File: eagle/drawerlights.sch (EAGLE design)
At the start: 12 parts

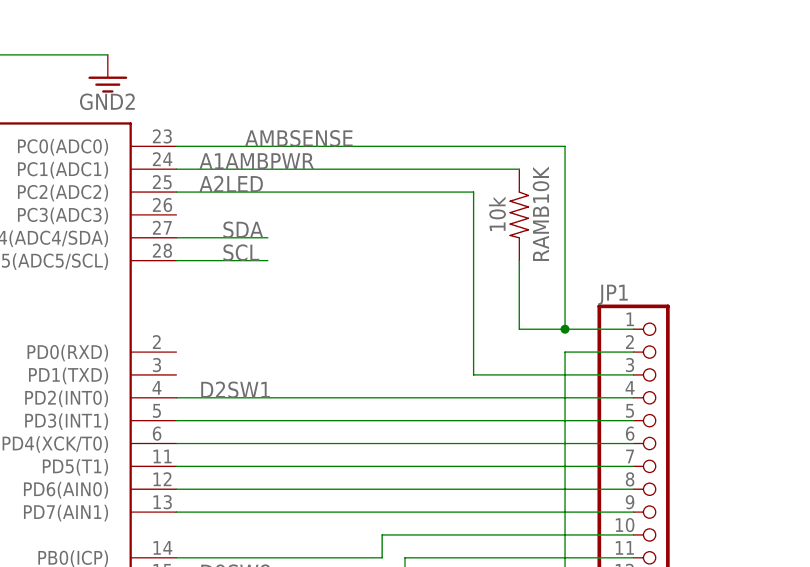
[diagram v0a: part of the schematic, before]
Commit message: add missing resistor for LED control
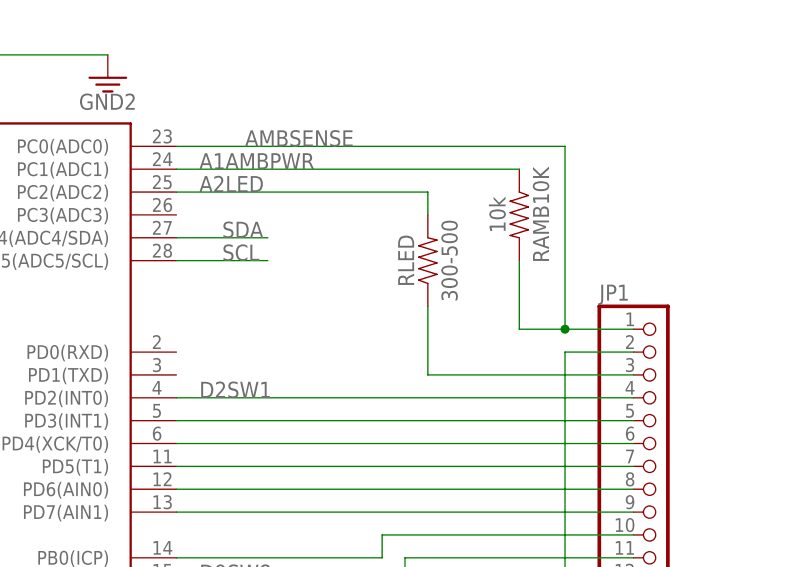
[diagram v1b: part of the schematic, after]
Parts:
- added RLED: 300-500, SparkFun-Resistors:330OHM-HORIZ-1/10W-5%
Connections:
- new net N$1: JP1.3, RLED.1
- net A2LED: now also RLED.2; no longer JP1.3
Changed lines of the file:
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@@
 <part name="LEDPWR" library="SparkFun-Connectors" deviceset="CONN_02" device=""/>
 <part name="C1" library="SparkFun-Capacitors" deviceset="100UF-POLAR" device="-RADIAL-2.5MM-25V-20%" value="100uF"/>
+<part name="RLED" library="SparkFun-Resistors" deviceset="330OHM" device="-HORIZ-1/10W-5%" value="300-500"/>
 </parts>
 <sheets>
@@
 <instance part="LEDPWR" gate="G$1" x="71.12" y="109.22"/>
 <instance part="C1" gate="G$1" x="83.82" y="119.38" rot="R90"/>
+<instance part="RLED" gate="G$1" x="99.06" y="71.12" rot="R90"/>
 </instances>
 <busses>
@@
 <segment>
 <pinref part="ATMEGA328" gate="G$1" pin="PC2(ADC2)"/>
-<wire x1="71.12" y1="78.74" x2="104.14" y2="78.74" width="0.1524" layer="91"/>
+<wire x1="71.12" y1="78.74" x2="99.06" y2="78.74" width="0.1524" layer="91"/>
 <label x="73.66" y="78.74" size="1.778" layer="95"/>
-<wire x1="104.14" y1="78.74" x2="104.14" y2="58.42" width="0.1524" layer="91"/>
-<pinref part="JP1" gate="G$1" pin="3"/>
-<wire x1="104.14" y1="58.42" x2="121.92" y2="58.42" width="0.1524" layer="91"/>
+<pinref part="RLED" gate="G$1" pin="2"/>
+<wire x1="99.06" y1="76.2" x2="99.06" y2="78.74" width="0.1524" layer="91"/>
 </segment>
 </net>
@@
 </segment>
 </net>
+<net name="N$1" class="0">
+<segment>
+<pinref part="JP1" gate="G$1" pin="3"/>
+<wire x1="99.06" y1="58.42" x2="121.92" y2="58.42" width="0.1524" layer="91"/>
+<pinref part="RLED" gate="G$1" pin="1"/>
+<wire x1="99.06" y1="66.04" x2="99.06" y2="58.42" width="0.1524" layer="91"/>
+</segment>
+</net>

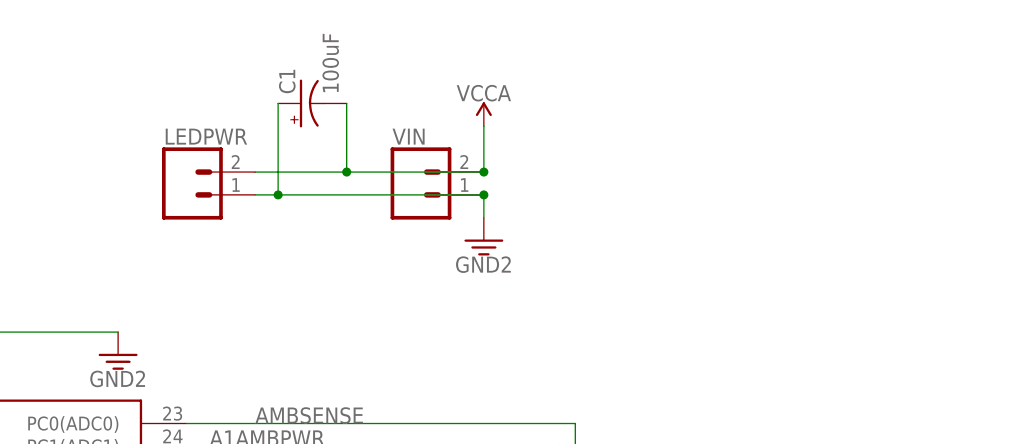
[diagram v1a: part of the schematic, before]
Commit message: fix vcc and LED power and filter cap polarity
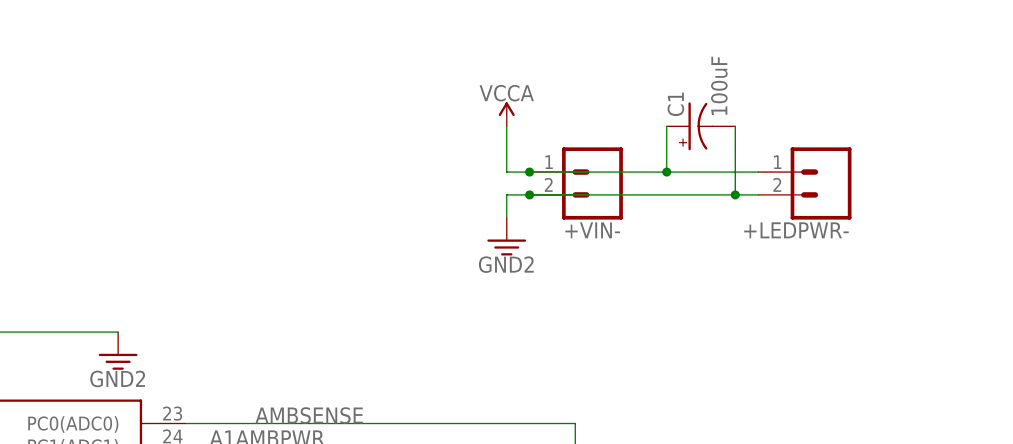
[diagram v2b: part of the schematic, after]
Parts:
- removed LEDPWR, VIN: (no value), SparkFun-Connectors:CONN_02
- added +LEDPWR-, +VIN-: (no value), SparkFun-Connectors:CONN_02
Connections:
- net GND: now also +LEDPWR-.2, +VIN-.2, C1.-; no longer C1.+, LEDPWR.1, VIN.1
- net VCCA: now also +LEDPWR-.1, +VIN-.1, C1.+; no longer C1.-, LEDPWR.2, VIN.2
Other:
- moved on the sheet: C1
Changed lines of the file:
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@@
 <part name="U$2" library="SparkFun-PowerSymbols" deviceset="VCCA" device=""/>
 <part name="SUPPLY4" library="SparkFun-PowerSymbols" deviceset="GND2" device=""/>
-<part name="VIN" library="SparkFun-Connectors" deviceset="CONN_02" device=""/>
+<part name="+VIN-" library="SparkFun-Connectors" deviceset="CONN_02" device=""/>
 <part name="SUPPLY6" library="SparkFun-PowerSymbols" deviceset="GND2" device=""/>
 <part name="RAMB10K" library="SparkFun-Resistors" deviceset="10KOHM" device="-HORIZ-1/4W-1%" value="10k"/>
@@
 <part name="JP1" library="adafruit" deviceset="PINHD-1X12" device="-CB"/>
 <part name="SUPPLY3" library="SparkFun-PowerSymbols" deviceset="GND2" device=""/>
-<part name="LEDPWR" library="SparkFun-Connectors" deviceset="CONN_02" device=""/>
+<part name="+LEDPWR-" library="SparkFun-Connectors" deviceset="CONN_02" device=""/>
 <part name="C1" library="SparkFun-Capacitors" deviceset="100UF-POLAR" device="-RADIAL-2.5MM-25V-20%" value="100uF"/>
 <part name="RLED" library="SparkFun-Resistors" deviceset="330OHM" device="-HORIZ-1/10W-5%" value="300-500"/>
@@
 <instance part="VCC" gate="G$1" x="5.08" y="83.82"/>
 <instance part="U$2" gate="G$1" x="12.7" y="96.52"/>
-<instance part="SUPPLY4" gate="GND" x="104.14" y="104.14"/>
-<instance part="VIN" gate="G$1" x="96.52" y="109.22"/>
+<instance part="SUPPLY4" gate="GND" x="106.68" y="104.14"/>
+<instance part="+VIN-" gate="G$1" x="116.84" y="111.76" rot="R180"/>
 <instance part="SUPPLY6" gate="GND" x="63.5" y="91.44"/>
 <instance part="RAMB10K" gate="G$1" x="109.22" y="76.2" rot="R270"/>
@@
 <instance part="TPDIV" gate="G$1" x="160.02" y="38.1"/>
 <instance part="TPVREG" gate="G$1" x="160.02" y="60.96"/>
-<instance part="U$1" gate="G$1" x="104.14" y="116.84"/>
+<instance part="U$1" gate="G$1" x="106.68" y="116.84"/>
 <instance part="JP1" gate="G$1" x="124.46" y="50.8"/>
 <instance part="SUPPLY3" gate="GND" x="114.3" y="33.02"/>
-<instance part="LEDPWR" gate="G$1" x="71.12" y="109.22"/>
-<instance part="C1" gate="G$1" x="83.82" y="119.38" rot="R90"/>
+<instance part="+LEDPWR-" gate="G$1" x="142.24" y="111.76" rot="R180"/>
+<instance part="C1" gate="G$1" x="127" y="116.84" rot="R90"/>
 <instance part="RLED" gate="G$1" x="99.06" y="71.12" rot="R90"/>
 </instances>
@@
 </segment>
 <segment>
-<pinref part="VIN" gate="G$1" pin="2"/>
+<pinref part="+VIN-" gate="G$1" pin="1"/>
+<wire x1="109.22" y1="111.76" x2="106.68" y2="111.76" width="0.1524" layer="91"/>
 <pinref part="U$1" gate="G$1" pin="VCCA"/>
-<wire x1="104.14" y1="111.76" x2="104.14" y2="116.84" width="0.1524" layer="91"/>
-<pinref part="LEDPWR" gate="G$1" pin="2"/>
-<wire x1="104.14" y1="111.76" x2="88.9" y2="111.76" width="0.1524" layer="91"/>
-<junction x="104.14" y="111.76"/>
-<pinref part="C1" gate="G$1" pin="-"/>
-<wire x1="88.9" y1="111.76" x2="78.74" y2="111.76" width="0.1524" layer="91"/>
-<wire x1="88.9" y1="119.38" x2="88.9" y2="111.76" width="0.1524" layer="91"/>
-<junction x="88.9" y="111.76"/>
+<wire x1="106.68" y1="111.76" x2="106.68" y2="116.84" width="0.1524" layer="91"/>
+<pinref part="+LEDPWR-" gate="G$1" pin="1"/>
+<wire x1="109.22" y1="111.76" x2="124.46" y2="111.76" width="0.1524" layer="91"/>
+<junction x="109.22" y="111.76"/>
+<pinref part="C1" gate="G$1" pin="+"/>
+<wire x1="124.46" y1="111.76" x2="134.62" y2="111.76" width="0.1524" layer="91"/>
+<wire x1="124.46" y1="116.84" x2="124.46" y2="111.76" width="0.1524" layer="91"/>
+<junction x="124.46" y="111.76"/>
 </segment>
 </net>
@@
 </segment>
 <segment>
-<pinref part="VIN" gate="G$1" pin="1"/>
-<pinref part="SUPPLY4" gate="GND" pin="3.3V"/>
-<wire x1="104.14" y1="109.22" x2="104.14" y2="106.68" width="0.1524" layer="91"/>
-<pinref part="LEDPWR" gate="G$1" pin="1"/>
-<wire x1="104.14" y1="109.22" x2="81.28" y2="109.22" width="0.1524" layer="91"/>
-<junction x="104.14" y="109.22"/>
-<pinref part="C1" gate="G$1" pin="+"/>
-<wire x1="81.28" y1="109.22" x2="78.74" y2="109.22" width="0.1524" layer="91"/>
-<wire x1="81.28" y1="119.38" x2="81.28" y2="109.22" width="0.1524" layer="91"/>
-<junction x="81.28" y="109.22"/>
-</segment>
-<segment>
 <pinref part="JP1" gate="G$1" pin="12"/>
 <pinref part="SUPPLY3" gate="GND" pin="3.3V"/>
@@
 <junction x="114.3" y="35.56"/>
 </segment>
+<segment>
+<pinref part="SUPPLY4" gate="GND" pin="3.3V"/>
+<wire x1="106.68" y1="106.68" x2="106.68" y2="109.22" width="0.1524" layer="91"/>
+<pinref part="+VIN-" gate="G$1" pin="2"/>
+<wire x1="109.22" y1="109.22" x2="106.68" y2="109.22" width="0.1524" layer="91"/>
+<pinref part="+LEDPWR-" gate="G$1" pin="2"/>
+<wire x1="134.62" y1="109.22" x2="132.08" y2="109.22" width="0.1524" layer="91"/>
+<junction x="109.22" y="109.22"/>
+<pinref part="C1" gate="G$1" pin="-"/>
+<wire x1="132.08" y1="109.22" x2="109.22" y2="109.22" width="0.1524" layer="91"/>
+<wire x1="132.08" y1="116.84" x2="132.08" y2="109.22" width="0.1524" layer="91"/>
+<junction x="132.08" y="109.22"/>
+</segment>
 </net>

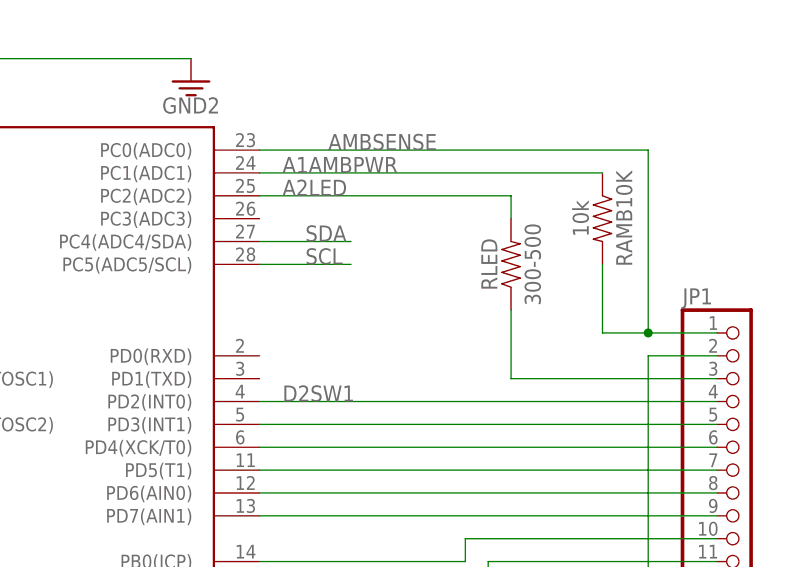
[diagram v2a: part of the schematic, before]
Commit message: move LED control to D0, fix # LEDs per drawer 4 => 8
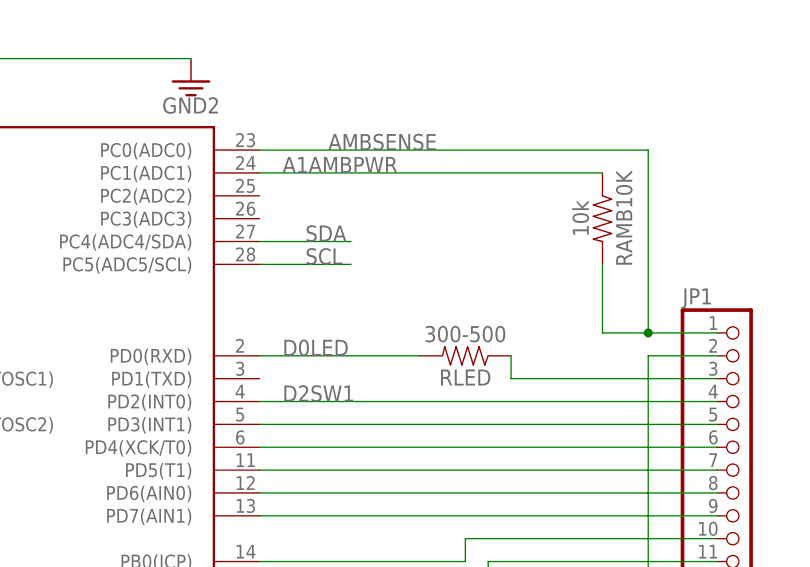
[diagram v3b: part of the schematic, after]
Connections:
- removed net A2LED: ATMEGA328.PC2(ADC2), RLED.2
- new net D0LED: ATMEGA328.PD0(RXD), RLED.2
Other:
- moved on the sheet: RLED
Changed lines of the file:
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@@
 <instance part="+LEDPWR-" gate="G$1" x="142.24" y="111.76" rot="R180"/>
 <instance part="C1" gate="G$1" x="127" y="116.84" rot="R90"/>
-<instance part="RLED" gate="G$1" x="99.06" y="71.12" rot="R90"/>
+<instance part="RLED" gate="G$1" x="93.98" y="60.96" rot="R180"/>
 </instances>
 <busses>
@@
 </segment>
 </net>
-<net name="A2LED" class="0">
-<segment>
-<pinref part="ATMEGA328" gate="G$1" pin="PC2(ADC2)"/>
-<wire x1="71.12" y1="78.74" x2="99.06" y2="78.74" width="0.1524" layer="91"/>
-<label x="73.66" y="78.74" size="1.778" layer="95"/>
-<pinref part="RLED" gate="G$1" pin="2"/>
-<wire x1="99.06" y1="76.2" x2="99.06" y2="78.74" width="0.1524" layer="91"/>
-</segment>
-</net>
 <net name="D2SW1" class="0">
 <segment>
@@
 <wire x1="99.06" y1="58.42" x2="121.92" y2="58.42" width="0.1524" layer="91"/>
 <pinref part="RLED" gate="G$1" pin="1"/>
-<wire x1="99.06" y1="66.04" x2="99.06" y2="58.42" width="0.1524" layer="91"/>
-</segment>
-</net>
+<wire x1="99.06" y1="60.96" x2="99.06" y2="58.42" width="0.1524" layer="91"/>
+</segment>
+</net>
+<net name="D0LED" class="0">
+<segment>
+<pinref part="RLED" gate="G$1" pin="2"/>
+<pinref part="ATMEGA328" gate="G$1" pin="PD0(RXD)"/>
+<wire x1="88.9" y1="60.96" x2="71.12" y2="60.96" width="0.1524" layer="91"/>
+<label x="73.66" y="60.96" size="1.778" layer="95"/>
+</segment>
+</net>
